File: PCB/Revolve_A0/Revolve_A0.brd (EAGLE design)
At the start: 100 x 100 mm, 409 parts, among them IC1 TMC2100-LA, IC12 TMC2100-LA, IC15 TMC2100-LA, IC2 TMC2100-LA, IC24 TMC2100-LA, IC29 LAN8710A, IC30 MTFC2GMDEA, IC31 CY7C65632, IC5 TMC2100-LA, IC6 74AHC1G126DCK, IC7 74AHC1G126DCK, Q1 AON6758, Q2 AON6758, Q3 AON6758, Q8 AON6758, U1 OSD3358-512M-BSM, U10 TPD4S012_DRY_6, U11 PCA9685PW, U19 CD4050BD, X1 22-05-7038-03, X10 22-05-7038-03, X11 22-05-7038-03, X12 22-05-7048-04, X13 22-05-7038-03, X14 22-05-7048-04, X15 22-05-7048-04, X16 22-05-7048-04, X17 22-05-7048-04, X18 22-05-7048-04, X19 22-05-7038-03, X2 MSTBA4, X20 MSTBA4, X21 MSTBA2, X22 22-05-7038-03, X24 HDMI, X25 22-05-7048-04, X26 MSTBA2, X29 22-05-7038-03, X3 MSTBA2, X4 22-05-7028-02, X5 22-05-7028-02, X6 22-05-7028-02, X7 22-05-7038-03, X8 22-05-7038-03, X9 22-05-7028-02, Y1 24MHz, Y3 25 MHz, Y4 12 MHz

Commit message: Working on the LAN layout
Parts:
- removed C106, C17, C19, C20, C22, C24, C27, C29, C31, C34, C43, C71: 0.1uF, rcl:C0402
- removed C116, C117, C118, C119, C120, C121, C122, C123, C124, C125, C126, C127, C128, C129, C130, C131: 47pF, rcl:C0402
- removed C139, C144, C145, C18, C21, C25, C36, C52, C62, C75, C76, C77, C78, C79, C81: 4.7uF, rcl:C0402
- removed C50: 10nF, rcl:C0402
- removed C90: 10uF, rcl:C0805
- removed C96: 100uF, Panasonic-EEEFK_EEEFP:RHS1V10MCN1GS
- removed IC1, IC12, IC15, IC2, IC24, IC5: TMC2100-LA, we-chip:QFN36-PAD
- removed IC31: CY7C65632, Revolve:QFN28
- removed R147: 0, DNI, rcl:R0402
- removed R148: 0, rcl:R0402
- removed R151: 10K, rcl:R0402
- removed R153: 22R, rcl:R0402
- removed R54, R86: 4.7K, rcl:R0402
- removed R91: 33, rcl:R0402
- removed U11: PCA9685PW, custom:SOP65P640X110-28N
- added C13: 0.1uF, rcl:C0402
- added C5: 18pF, rcl:C0402
- added H1, H2, H3, H4: MOUNT-HOLE3.2, holes:3,2
- added J1: (no value), OSD3358-SM-RED Platform:CTI-JTAG
- added Q9: MMBT2907, OSD3358-SM-RED Platform:SOT23-BEC
- added R143, R144: 4.7K, rcl:R0402
- added R26: 1M, rcl:R0402
- added SV3: (no value), con-lstb:MA04-2
- added SV4: (no value), con-lstb:MA03-1
- added SV5: (no value), con-lstb:MA04-1
- added U$13, U$14, U$15, U$16: TRINAMIC_TMC2130_QFN36, TMC2130-Eval_v13:TRINAMIC_QFN36
- added U2: TUSB2046BIRHBT, Texas Instruments_By_element14_Batch_1:QFN50P500X500X100-33N
- added U3, U4: TPD2E001DRSR, Texas Instruments_By_element14_Batch_1:SON95P315X315X80-7N
- added U5: SN74HC245DW, Texas Instruments_By_element14_Batch_1:SOIC127P1030X265-20N
- added U7: TLVH431, OSD3358-SM-RED Platform:SOT23-3
- added Y5: ABS07-32.768KHZ-T, OSD3358-SM-RED Platform:CRYSTAL_3.2X1.5
- C1: value 22nF -> 0.1uF
- C12, C138, C140, C141, C142: value 4.7uF -> 0.1uF
- C143: value 4.7uF -> 10uF
- C48, C80: value 10uF -> 22uF
- C6: value 0.1uF -> 18pF
- EEPROM_WP, PMIC_NRESET, SYS_5V, SYS_RTC_1V8, SYS_VDD1_3V3, SYS_VDD2_3V3, SYS_VDD3_3V3, VDDS_DDR, VDDS_PLL, VDD_CODE, VDD_MPU: value TPPAD1-13 -> TPB1,27; device testpad:P1-13 -> testpad:B1,27
- R1: value 0.1R -> 1.5K; device rcl:R0805 -> rcl:R0402
- R12: value 44.3K,1% -> 100K,1%
- R152: value 10K -> 10K,1%
- R2: value 0.1R -> 0,DNI; device rcl:R0805 -> rcl:R0402
- R22: value 10K,1% -> 13.3K,1%
- R24: value 4.7K -> 0R,DNI
- R41: value 10K -> 10K, 1%; device rcl:R0402 -> OSD3358-SM-RED Platform:R0402
- R49: value 10K -> 40.2K, 1%; device rcl:R0402 -> OSD3358-SM-RED Platform:R0402
- R53: value 2.2R -> 499; device rcl:R0402 -> OSD3358-SM-RED Platform:R0402
- R87: value 650R, 1% -> 4.7K
- SV2: device con-lstb:MA05-1 -> con-lstb:MA04-2
- U$9: value SN74AUC1G74DCTR -> TRINAMIC_TMC2130_QFN36; device Revolve:S-PDSO-G8 -> TMC2130-Eval_v13:TRINAMIC_QFN36
- Y1: value 24MHz -> 25MHz
- Y4: value 12 MHz -> 6 MHz
- moved PMIC_NRESET 474.8 mm to (44.7, 69.9), flipped to the bottom
- moved VDDS_PLL 452.8 mm to (38.5, 70.0), flipped to the bottom
- moved VDD_MPU 431.2 mm to (37.0, 70.0), flipped to the bottom
- moved VDD_CODE 397.7 mm to (38.8, 57.7), flipped to the bottom
- moved VDDS_DDR 376.0 mm to (37.3, 57.7), flipped to the bottom
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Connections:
- net N$1 renamed PMIC_PWR_EN
- net N$103 renamed PMIC_SCL
- net N$104 renamed PMIC_SDA
- net N$121 renamed PMIC_LDO_PGOOD
- net N$143 renamed PMIC_NWAKEUP
- net N$144 renamed PMIC_NINT
- net N$157 renamed TXP
- net N$158 renamed TXN
- net N$159 renamed RXP
- net N$160 renamed RXN
- net N$174 renamed EEPROM_WP
- net VBUS renamed USB_HOST_5V
- removed net 12MHZ: R91.1, U$7.27
- removed net D+: U$8.P$3, U10.1
- removed net D-: U$8.P$2, U10.2
- removed net ENABLE_A: IC24.22
- removed net ENABLE_E: IC12.22
- removed net ENABLE_H: IC15.22
- removed net ENABLE_X: IC1.22, U$2.22
- removed net ENABLE_Y: IC2.22
- removed net ENABLE_Z: IC5.22
- removed net END_STOP_X_1: U19.2
- removed net END_STOP_X_2: U19.10
- removed net END_STOP_Y_1: U19.4
- removed net END_STOP_Y_2: U19.12
- removed net END_STOP_Z_1: U19.6
- removed net END_STOP_Z_2: U19.15
- removed net FAULT_X0: U$2.20
- removed net FAULT_X1: U$2.21
- removed net I2C2_SCL: U11.26
- removed net I2C2_SDA: U11.27
- removed net ID: U$8.P$4, U10.3
- removed net IREF_A_RAW: R73.2, U11.8
- removed net IREF_E_RAW: R60.2, U11.21
- removed net IREF_H1: C81.1, R43.2, R73.1
- removed net IREF_H_RAW: R31.2, U11.22
- removed net IREF_X1: C145.1, R140.2, R141.1
- removed net IREF_X_RAW: R141.2, R41.2, U11.18
- removed net IREF_Y_RAW: R37.2, U11.19
- removed net IREF_Z_RAW: R58.2, U11.20
- removed net N$100: IC15.5
- removed net N$101: IC15.18
- removed net N$102: IC15.19
- removed net N$105: SYS_VDD1_3V3.TP, U1.F6, U1.F7, U1.G6, U1.G7
- removed net N$107: C70.1, IC15.26, R52.2
- removed net N$108: C71.1, IC1.26, R53.2
- removed net N$110: C72.1, IC2.26, R59.2
- removed net N$111: C74.1, IC12.26, R71.2
- removed net N$112: IC12.32, X17.1
- removed net N$119: IC15.32, X18.1
- removed net N$120: SYS_VDD3_3V3.TP, U1.F8, U1.G8, U1.H7, U1.H8, U1.J7, U1.J8, U1.K8, U1.L8
- removed net N$131: C52.1, IC24.23, R43.1
- removed net N$133: IC24.3
- removed net N$135: IC24.34, X25.2
- removed net N$136: C55.2, IC24.25, R72.1
- removed net N$138: IC24.4
- removed net N$139: IC24.5
- removed net N$140: IC24.18
- removed net N$141: IC24.19
- removed net N$142: SYS_RTC_1V8.TP, U1.K11, U1.L11
- removed net N$146: U1.F9, U1.G9, U1.H9, U1.J9, U1.K9, U1.L9
- removed net N$148: IC24.32, X25.1
- removed net N$165: U1.T7
- removed net N$166: C86.2, R126.1, U$2.25
- removed net N$175: R86.2
- removed net N$178: U1.T16
- removed net N$18: IC1.14, R1.2
- removed net N$185: C144.1, R140.1, U$2.23
- removed net N$186: U1.T12
- removed net N$187: C155.1, IC31.27, R147.1, R148.1
- removed net N$188: U1.R12
- removed net N$190: U1.T13
- removed net N$191: IC31.14, IC31.21, IC31.28, IC31.5, IC31.9
- removed net N$197: IC31.13, U$6.3
- removed net N$198: IC31.12, U$6.2
- removed net N$199: IC31.16, U$6.7
- removed net N$200: IC31.15, U$6.6
- removed net N$202: U$9.2, U$9.3
- removed net N$205: R91.2, U$9.5
- removed net N$210: SV2.5, U1.B12
- removed net N$213: C157.2, IC31.11, Y4.P$1
- removed net N$215: SV2.4, U1.A12
- removed net N$26: C25.1, IC5.23, R27.1
- removed net N$31: C21.2, IC1.25, R53.1
- removed net N$47: C33.2, IC2.25, R59.1
- removed net N$50: IC5.34, X16.2
- removed net N$51: C37.2, IC5.25, R70.1
- removed net N$53: IC2.5
- removed net N$54: IC5.4
- removed net N$55: IC5.5
- removed net N$56: IC2.18
- removed net N$57: IC5.18
- removed net N$58: IC5.19
- removed net N$60: C50.2, L1.P$2, U$10.2
- removed net N$65: IC2.19
- removed net N$73: C50.1, U$10.6
- removed net N$74: C62.1, IC12.23, R35.1
- removed net N$76: IC12.3
- removed net N$78: IC12.34, X17.2
- removed net N$79: C65.2, IC12.25, R71.1
- removed net N$81: IC12.4
- removed net N$82: IC12.5
- removed net N$83: IC12.18
- removed net N$84: IC12.19
- removed net N$89: C36.1, IC15.23, R50.1
- removed net N$91: IC15.3
- removed net N$94: IC15.34, X18.2
- removed net N$95: C68.2, IC15.25, R52.1
- removed net N$99: IC15.4
- removed net SPI0_CS0: U1.A14
- removed net SPI0_CS1: U1.C14
- removed net USB1_OCN: U1.R15
- removed net XDMA_EVENT_INTR0: U$9.1, U1.A4
- removed net X_CFG1: IC1.4
- removed net X_CFG2: IC1.3
- new net 5VIN_Y: C72.1, R59.2, U$13.26
- new net 5VOUT_A: C55.2, R72.1, R73.2, U$16.25
- new net 5VOUT_E: C65.2, R35.2, R71.1, U$14.25
- new net 5VOUT_H: C68.2, R31.2, R52.1, U$15.25
- new net 5VOUT_X: C86.2, R126.1, R140.2, U$2.25
- new net 5VOUT_Y: C33.2, R37.2, R59.1, U$13.25
- new net 5VOUT_Z: C37.2, R27.2, R70.1, U$9.25
- new net CLKOUT1_25MHZ: R2.1, U1.A4
- new net CLKOUT2_48MHZ: U1.B4, U2.27
- new net ECAP1: SV5.3, U1.B12
- new net ECAP2: SV5.2, U1.A12
- new net EHRPWM1A: U1.P12, U5.6
- new net EHRPWM1B: U1.T13, U5.7
- new net EHRPWM2A: U1.T4, U5.8
- new net EHRPWM2B: U1.P5, U5.9
- new net EMU0: J1.13, U1.E2
- new net EMU1: J1.14, U1.E3
- new net ENABLE_B: SV2.4
- new net ENABLE_C: SV3.3
- new net END_STOP_X1: U1.N14, U19.2
- new net END_STOP_X2: U1.R12, U19.10
- new net END_STOP_Y1: U1.T16, U19.4
- new net END_STOP_Y2: U1.P3, U19.12
- new net END_STOP_Z1: U1.T6, U19.6
- new net END_STOP_Z2: U1.P7, U19.15
- new net FAULT_A: R44.1, U$16.20, U$16.21
- new net FAULT_B: SV2.2
- new net FAULT_C: SV3.1
- new net GPIO0_18: U1.J15
- new net GPIO0_26: U1.R5
- new net I2C1_SCL: U1.B11
- new net I2C1_SDA: U1.A11
- new net N$1: R41.1, R49.2, U7.1
- new net N$25: R152.1, U1.M16
- new net QUAD_ENCODER_A: U1.R13
- new net QUAD_ENCODER_B: U1.P13
- new net SPI0_CSA: U$16.2, U1.J14
- new net SPI0_CSE: U$14.2, U1.T12
- new net SPI0_CSH: U$15.2, U1.R7
- new net SPI0_CSY: U$13.2, U1.C14
- new net SPI0_CSZ: U$9.2, U1.T7
- new net SPI1_CS0: SV3.4, U1.B10
- new net SPI1_CS1: SV2.3, U1.A10
- new net SPI1_MISO: SV2.6, SV3.6, U1.C12
- new net SPI1_MOSI: SV2.8, SV3.8, U1.C13
- new net SPI1_SCLK: SV2.1, SV3.2, U1.C5
- new net SW: C2.1, L1.P$2, U$10.2
- new net SYS_RTC_1V8: Q9.C, R49.1, SYS_RTC_1V8.TP, U1.K11, U1.L11, U7.3
- new net SYS_VDD1_3V3: C13.1, C140.1, C141.1, C142.1, C143.1, C150.1, C155.1, IC29.12, IC30.C6, IC30.E6, IC30.F5, IC30.J10, IC30.K9, IC30.M4, IC30.N4, IC30.P3, IC30.P5, L2.1, R1.2, R127.2, R128.2, R129.2, R130.2, R131.2, R132.2, R133.2, R134.2, R135.2, R136.2, R137.2, R24.1, R85.1, R88.2, SYS_VDD1_3V3.TP, U1.F6, U1.F7, U1.G6, U1.G7, U2.25, U2.26, U2.3
- new net SYS_VDD3_3V3: Q9.E, R41.2, R53.2, SYS_VDD3_3V3.TP, U1.F8, U1.F9, U1.G8, U1.G9, U1.H7, U1.H8, U1.H9, U1.J7, U1.J8, U1.J9, U1.K8, U1.K9, U1.L8, U1.L9
- new net TCK: J1.11, U1.D1
- new net TDI: J1.3, U1.C1
- new net TDO: J1.7, U1.C2
- new net TIMER4: U1.M1, U5.2
- new net TIMER5: U1.N3, U5.3
- new net TIMER6: U1.N2, U5.4
- new net TIMER7: U1.N1, U5.5
- new net TK_A: U1.D7
- new net TK_E: U1.C7
- new net TK_H: U1.C8
- new net TK_HBP: U1.C9
- new net TMS: J1.1, U1.D2
- new net TRSRTN: J1.2
- new net TRSTN: U1.D3
- new net UART4_RXD: SV4.1, U1.P15
- new net UART4_TXD: SV4.2, U1.R16
- new net USB1_DM3: U$6.2, U2.19, U4.3
- new net USB1_DM4: U$6.6, U2.23, U3.3
- new net USB1_DP3: U$6.3, U2.20, U4.6
- new net USB1_DP4: U$6.7, U2.24, U3.6
- new net USB_XTAL1: C157.2, U2.30, Y4.P$1
- new net VCC: U3.1, U4.1
- new net VCC_E: C74.1, R71.2, U$14.26
- new net VCC_H: C70.1, R52.2, U$15.26
- net +24V: now also C1.2, U$13.16, U$13.30, U$13.31, U$14.16, U$14.30, U$14.31, U$15.16, U$15.30, U$15.31, U$16.16, U$16.30, U$16.31, U$9.16, U$9.30, U$9.31; no longer C19.1, C20.2, C22.2, C24.1, C27.1, C29.1, C31.1, C34.1, C43.1, C6.1, C90.1, C96.+, IC1.16, IC1.30, IC1.31, IC12.16, IC12.30, IC12.31, IC15.16, IC15.30, IC15.31, IC2.16, IC2.30, IC2.31, IC24.16, IC24.30, IC24.31, IC5.16, IC5.30, IC5.31
- net +3V3: now also R143.1, R144.1, U$13.8, U$14.8, U$15.8, U$16.8; no longer C106.1, C2.1, IC1.8, IC12.8, IC15.8, IC2.8, IC24.8, IC5.8, R24.2, R54.2, U$9.6, U$9.7
- net +5V: no longer R147.2
- net CGND: now also U$3.SHD1, U$3.SHD2, U$5.A10, U$5.A11, U$5.A12, U$5.A9, U$6.A10, U$6.A11, U$6.A12, U$6.A9, U$8.P$10, U$8.P$11, U$8.P$6, U$8.P$7, U$8.P$8, U$8.P$9, X24.PAD1, X24.PAD2, X24.PAD3, X24.PAD4
- net DIR_A: now also U$16.7; no longer IC24.7
- net DIR_B: now also SV2.5
- net DIR_C: now also SV3.5
- net DIR_E: now also U$14.7; no longer IC12.7
- net DIR_H: now also U$15.7; no longer IC15.7
- net DIR_X: no longer IC1.7
- net DIR_Y: now also U$13.7; no longer IC2.7
- net DIR_Z: now also U$9.7; no longer IC5.7
- net EMMC_RST: no longer U1.R13
- net ENABLE: now also U5.19; no longer U11.23
- net FAN0: now also U5.14; no longer U11.13
- net FAN1: now also U5.13; no longer U11.15
- net FAN2: now also U5.12; no longer U11.16
- net FAN3: now also U5.11; no longer U11.17
- net FAULT_E: now also U$14.20, U$14.21; no longer IC12.20
- net FAULT_H: now also U$15.20, U$15.21; no longer IC15.20, IC24.20, R44.1
- net FAULT_X: now also R143.2, U$2.20, U$2.21, U1.T5; no longer IC1.20, R54.1
- net FAULT_Y: now also R144.2, U$13.20, U$13.21; no longer IC2.20, R24.1
- net FAULT_Z: now also U$9.20, U$9.21; no longer IC5.20
- net GND: now also C1.1, C13.2, J1.10, J1.12, J1.16, J1.20, J1.8, R141.1, R152.2, R43.1, R50.1, R58.1, R6.1, R60.1, SV4.3, SV5.1, U$13.1, U$13.11, U$13.12, U$13.17, U$13.22, U$13.24, U$13.35, U$13.36, U$13.9, U$13.GND_PAD, U$14.1, U$14.11, U$14.12, U$14.17, U$14.22, U$14.24, U$14.35, U$14.36, U$14.9, U$14.GND_PAD, U$15.1, U$15.11, U$15.12, U$15.17, U$15.22, U$15.24, U$15.35, U$15.36, U$15.9, U$15.GND_PAD, U$16.1, U$16.11, U$16.12, U$16.17, U$16.22, U$16.24, U$16.35, U$16.36, U$16.9, U$16.GND_PAD, U$2.22, U$2.9, U$9.1, U$9.11, U$9.12, U$9.17, U$9.22, U$9.24, U$9.35, U$9.36, U$9.9, U$9.GND_PAD, U2.28, U2.7, U2.8, U5.10; no longer C106.2, C116.2, C117.2, C118.2, C119.2, C120.2, C121.2, C122.2, C123.2, C124.2, C125.2, C126.2, C127.2, C128.2, C129.2, C130.2, C131.2, C139.2, C144.2, C145.2, C17.2, C18.2, C19.2, C2.2, C20.1, C21.1, C24.2, C25.2, C27.2, C29.2, C31.2, C34.2, C36.2, C43.2, C52.2, C6.2, C62.2, C71.2, C75.2, C76.2, C77.2, C78.2, C79.2, C81.2, C90.2, C96.-, IC1.1, IC1.10, IC1.11, IC1.12, IC1.24, IC1.35, IC1.36, IC1.TP, IC12.1, IC12.10, IC12.11, IC12.12, IC12.24, IC12.35, IC12.36, IC12.TP, IC15.1, IC15.10, IC15.11, IC15.12, IC15.24, IC15.35, IC15.36, IC15.TP, IC2.1, IC2.10, IC2.11, IC2.12, IC2.24, IC2.35, IC2.36, IC2.TP, IC24.1, IC24.10, IC24.11, IC24.12, IC24.24, IC24.35, IC24.36, IC24.TP, IC31.29, IC5.1, IC5.10, IC5.11, IC5.12, IC5.24, IC5.35, IC5.36, IC5.TP, R1.1, R151.1, R2.1, R86.1, SV2.1, U$5.A10, U$5.A11, U$5.A12, U$5.A9, U$6.A10, U$6.A11, U$6.A12, U$6.A9, U$8.P$10, U$8.P$11, U$8.P$6, U$8.P$7, U$8.P$8, U$8.P$9, U$9.4, U11.14
- net HDMI_1V8: now also C12.1
- net HDMI_INT: now also U1.R15; no longer U1.T15
- net HEATER_A: now also U5.15; no longer U11.12
- net HEATER_E: now also U5.18; no longer U1.P12
- net HEATER_H: now also U5.17; no longer U11.9
- net HEATER_HBP: now also U5.16; no longer U11.10
- net IREF_E: now also R35.1, R60.2, U$14.23; no longer C79.1, R35.2, R60.1
- net IREF_H: now also U$15.23; no longer C75.1
- net IREF_X: now also R140.1, R141.2, U$2.23; no longer C77.1, R41.1, R49.2
- net IREF_Y: now also U$13.23; no longer C76.1
- net IREF_Z: now also R27.1, R58.2, U$9.23; no longer C78.1, R27.2, R58.1
- net LCD_D0: no longer C116.1
- net LCD_D1: no longer C117.1
- net LCD_D10: no longer C126.1
- net LCD_D11: no longer C127.1
- net LCD_D12: no longer C128.1
- net LCD_D13: no longer C129.1
- net LCD_D14: no longer C130.1
- net LCD_D15: no longer C131.1
- net LCD_D2: no longer C118.1
- net LCD_D3: no longer C119.1
- net LCD_D4: no longer C120.1
- net LCD_D5: no longer C121.1
- net LCD_D6: no longer C122.1
- net LCD_D7: no longer C123.1
- net LCD_D8: no longer C124.1
- net LCD_D9: no longer C125.1
- net LCD_DE: no longer R153.2
- net LCD_PCLK: no longer R153.1
- net N$109: now also U$9.26; no longer IC5.26
- net N$113: now also U$15.13; no longer IC15.13
- net N$12: now also U$15.27; no longer IC15.27
- net N$126: now also U$16.14; no longer IC24.14
- net N$128: now also U$16.33; no longer IC24.33
- net N$13: now also U$15.14; no longer IC15.14
- net N$132: now also U$16.28; no longer IC24.28
- net N$134: now also U$16.15; no longer IC24.15
- net N$137: now also U$16.29; no longer IC24.29
- net N$14: now also U$9.27; no longer IC5.27
- net N$145: now also U$16.26; no longer IC24.26
- net N$147: now also U$16.13; no longer IC24.13
- net N$15: now also U$9.14; no longer IC5.14
- net N$16: now also U$9.32, X16.2; no longer C1.1, IC1.28
- net N$17: now also U2.10, U2.14, U2.18, U2.22; no longer C1.2, IC1.27
- net N$180: now also R2.2
- net N$19: now also U$13.32, X15.2; no longer IC1.33, R2.2
- net N$192: now also R24.2, U2.31; no longer IC31.8
- net N$193: now also U2.12; no longer IC31.4
- net N$194: now also U2.11; no longer IC31.3
- net N$195: now also U2.16; no longer IC31.7
- net N$196: now also U2.15; no longer IC31.6
- net N$2: now also U$13.13; no longer IC2.13
- net N$20: now also U$13.34, X15.1; no longer C12.1, IC1.23, R49.1
- net N$214: now also U2.29; no longer IC31.10
- net N$22: now also U$14.34, X17.1; no longer IC2.32, X15.1
- net N$24: now also U$9.33; no longer IC5.33
- net N$27: now also U$9.28; no longer IC5.28
- net N$28: now also U$14.32, X17.2; no longer IC5.3
- net N$29: now also U$9.15; no longer IC5.15
- net N$3: now also U$13.27; no longer IC2.27
- net N$30: now also U$15.33; no longer IC15.33
- net N$32: now also U$15.34, X18.1; no longer IC5.32, X16.1
- net N$33: now also C5.1, C6.1, U1.B5; no longer C22.1, IC1.29
- net N$35: now also U$13.14; no longer IC2.14
- net N$36: now also U$13.33; no longer IC2.33
- net N$37: now also U$9.13; no longer IC5.13
- net N$38: now also U$15.32, X18.2; no longer C18.1, IC2.23, R6.1
- net N$39: now also U$14.13; no longer IC12.13
- net N$4: now also Q9.B, R53.1, U7.2; no longer SV2.3, U1.C12
- net N$41: now also U$13.28; no longer IC2.28
- net N$42: now also C6.2, R26.2, U1.A5, Y5.P$2; no longer IC2.3
- net N$43: now also C5.2, R26.1, U1.A6, Y5.P$1; no longer IC1.19
- net N$44: now also U$16.34, X25.1; no longer IC1.5
- net N$45: now also U$13.15; no longer IC2.15
- net N$46: now also U$16.32, X25.2; no longer IC2.34, X15.2
- net N$48: now also U$13.29; no longer IC2.29
- net N$49: now also R43.2, R73.1, U$16.23; no longer IC2.4
- net N$5: now also C2.2, U$10.6; no longer SV2.2, U1.C13
- net N$52: now also U$9.29; no longer IC5.29
- net N$6: now also U$9.34, X16.1; no longer IC1.18
- net N$70: now also U$14.27; no longer IC12.27
- net N$71: now also U$14.14; no longer IC12.14
- net N$72: now also U$14.33; no longer IC12.33
- net N$75: now also U$14.28; no longer IC12.28
- net N$77: now also U$14.15; no longer IC12.15
- net N$80: now also U$14.29; no longer IC12.29
- net N$90: now also U$15.28; no longer IC15.28
- net N$92: now also U$15.15; no longer IC15.15
- net N$96: now also U$16.27; no longer IC24.27
- net N$98: now also U$15.29; no longer IC15.29
- net SPI0_CSX: now also U1.A14
- net SPI0_MISO: now also U$13.5, U$14.5, U$15.5, U$16.5, U$9.5
- net SPI0_MOSI: now also U$13.4, U$14.4, U$15.4, U$16.4, U$9.4
- net SPI0_SCLK: now also U$13.3, U$14.3, U$15.3, U$16.3, U$9.3
- net STEP_A: now also U$16.6; no longer IC24.6
- net STEP_B: now also SV2.7
- net STEP_C: now also SV3.7
- net STEP_E: now also U$14.6; no longer IC12.6
- net STEP_H: now also U$15.6; no longer IC15.6
- net STEP_X: no longer IC1.6
- net STEP_Y: now also U$13.6; no longer IC2.6
- net STEP_Z: now also U$9.6; no longer IC5.6
- net SYS_5V: now also U5.1, U5.20; no longer C17.1, R148.2, R88.2, U11.1, U11.2, U11.24, U11.28, U11.3, U11.4, U11.5
- net SYS_RESETN: now also U1.N12, U1.P11, U1.R11
- net SYS_VDD2_3V3: now also SV5.4
- net USB0_DM: now also U$8.P$2, U10.2
- net USB0_DP: now also U$8.P$3, U10.1
- net USB0_ID: now also U$8.P$4, U10.3
- net USB1_DM: now also U2.2; no longer IC31.1
- net USB1_DP: now also R1.1, U2.1; no longer IC31.2
- net USB_DC: no longer IC31.22, R151.2
- net USB_RESET: now also U2.4; no longer IC31.17
- net USR0: now also U1.T15; no longer U1.P13
- net VDD_3V3B: no longer C139.1, C140.1, C141.1, C142.1, C143.1, C150.1, IC29.12, IC30.C6, IC30.E6, IC30.F5, IC30.J10, IC30.K9, IC30.M4, IC30.N4, IC30.P3, IC30.P5, L2.1, R127.2, R128.2, R129.2, R130.2, R131.2, R132.2, R133.2, R134.2, R135.2, R136.2, R137.2, R85.1
- net X_A1: now also X14.1; no longer X14.2
- net X_A2: now also X14.2; no longer X14.1
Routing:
- net SPI0_MISO: track 0.00 -> 164.0 mm, vias 0 -> 7
- net FAN3: track 148.3 -> 0.00 mm, vias 2 -> 0
- net FAN2: track 141.6 -> 0.00 mm, vias 2 -> 0
- net FAN1: track 136.2 -> 0.00 mm, vias 2 -> 0
- net FAN0: track 135.4 -> 0.00 mm, vias 4 -> 0
- net SYS_RESETN: track 12.6 -> 141.1 mm, vias 0 -> 5
- net SPI0_MOSI: track 0.00 -> 125.8 mm, vias 0 -> 6
- net SPI0_SCLK: track 0.00 -> 121.9 mm, vias 0 -> 6
- net IREF_A_RAW: track 113.0 -> 0.00 mm, vias 4 -> 0
- net SYS_5V: track 94.9 -> 0.64 mm, vias 4 -> 1
- net IREF_H_RAW: track 82.0 -> 0.00 mm, vias 2 -> 0
- net N$125: track 1.12 -> 76.7 mm, vias 0 -> 2
- net N$124: track 1.18 -> 75.7 mm, vias 0 -> 2
- net N$123: track 1.18 -> 74.7 mm, vias 0 -> 2
- net N$201: track 0.00 -> 73.0 mm, vias 0 -> 2
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- added copper zone on layer 1, net +5V
- added copper zone on layer 3, net N$18
- added copper zone on layer 1, net SW
- added copper zone on layer 3, net SW
- added copper zone on layer 1, net SYS_5V
- added copper zone on layer 1, net SYS_RTC_1V8
- added copper zone on layer 1, net SYS_VDD1_3V3
- added copper zone on layer 3, net SYS_VDD1_3V3
- added copper zone on layer 1, net SYS_VDD2_3V3
- added copper zone on layer 1, net SYS_VDD3_3V3
- added copper zone on layer 1, net SYS_VDD_1V8
- added copper zone on layer 1, net USB_DC
- added copper zone on layer 1, net VIN_BAT
- removed copper zone on layer 3, net VDD_3V3B
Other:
- outline, holes or cut-outs redrawn

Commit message: Working on layout
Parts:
- removed C5, C6: 18pF, rcl:C0402
- removed R26, R84: 1M, rcl:R0402
- removed U5: SN74HC245DW, Texas Instruments_By_element14_Batch_1:SOIC127P1030X265-20N
- removed Y3: 25 MHz, Revolve:ECS-250-20-5PVX
- removed Y5: ABS07-32.768KHZ-T, OSD3358-SM-RED Platform:CRYSTAL_3.2X1.5
- added Y2: 25MHz, Revolve:445C33D24M00000
- moved C61 41.5 mm to (64.7, 90.0), turned to 270 degrees
- moved U19 36.5 mm to (59.0, 88.2), turned to 270 degrees
- moved C151 30.0 mm to (28.9, 66.0)
- moved C152 29.6 mm to (28.9, 64.9)
- moved C107 29.2 mm to (28.9, 63.8)
- moved C148 6.83 mm to (30.8, 82.2), turned to 270 degrees
- moved C149 5.30 mm to (30.8, 86.8), turned to 90 degrees
- moved R95 1.81 mm to (32.5, 77.1)
- moved R96 1.81 mm to (33.6, 77.1)
- moved R100 1.81 mm to (31.5, 77.1)
- moved R101 1.81 mm to (36.8, 77.1)
- moved R103 1.81 mm to (38.8, 77.1)
- moved R104 1.81 mm to (37.8, 77.1)
- moved R85 1.81 mm to (39.8, 77.1)
- moved R97 1.81 mm to (34.7, 77.1)
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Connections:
- removed net +3V3: C23.1, C30.1, C44.1, C53.1, C61.1, C63.1, C84.1, R114.2, R117.2, R118.2, R119.2, R120.2, R143.1, R144.1, R28.2, R36.2, R44.2, R51.2, U$13.8, U$14.8, U$15.8, U$16.8, U$2.8, U$9.8, U19.1
- removed net ENABLE: U5.19
- removed net N$33: C5.1, C6.1, U1.B5
- removed net N$42: C6.2, R26.2, U1.A5, Y5.P$2
- removed net N$43: C5.2, R26.1, U1.A6, Y5.P$1
- net EHRPWM1A: no longer U5.6
- net EHRPWM1B: no longer U5.7
- net EHRPWM2A: no longer U5.8
- net EHRPWM2B: no longer U5.9
- net FAN0: no longer U5.14
- net FAN1: no longer U5.13
- net FAN2: no longer U5.12
- net FAN3: no longer U5.11
- net GND: now also X11.3, X7.3, X8.3; no longer U5.10
- net HEATER_A: no longer U5.15
- net HEATER_E: no longer U5.18
- net HEATER_H: no longer U5.17
- net HEATER_HBP: no longer U5.16
- net N$151: now also X11.2
- net N$180: now also Y2.P$2; no longer R84.2, Y3.P$2
- net N$181: now also Y2.P$1; no longer Y3.P$1
- net N$183: no longer R84.1
- net N$237: now also X8.2
- net N$241: now also X7.2
- net SYS_5V: no longer U5.1, U5.20
- net SYS_VDD1_3V3: now also C23.1, C30.1, C44.1, C53.1, C61.1, C63.1, C84.1, R114.2, R117.2, R118.2, R119.2, R120.2, R143.1, R144.1, R28.2, R36.2, R44.2, R51.2, U$13.8, U$14.8, U$15.8, U$16.8, U$2.8, U$9.8, U19.1
- net TIMER4: no longer U5.2
- net TIMER5: no longer U5.3
- net TIMER6: no longer U5.4
- net TIMER7: no longer U5.5
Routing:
- net SYS_VDD1_3V3: track 41.1 -> 160.0 mm, vias 19 -> 31
- net +3V3: track 118.3 -> 0.00 mm, vias 12 -> 0
- net TERM_A: track 0.00 -> 51.7 mm, vias 0 -> 2
- net SPI0_SCLK: track 121.9 -> 169.1 mm, vias 6 -> 7
- net SPI0_MOSI: track 125.8 -> 170.6 mm, vias 6 -> 8
- net SPI0_CSX: track 15.7 -> 58.2 mm, vias 0 -> 2
- net N$155: track 80.5 -> 40.9 mm
- net TERM_HBP: track 0.00 -> 33.1 mm, vias 0 -> 1
- net END_STOP_Z_2_IN: track 2.31 -> 30.1 mm, vias 0 -> 1
- net END_STOP_Y_2_IN: track 2.94 -> 26.9 mm, vias 0 -> 2
- net STEP_E: track 38.3 -> 61.8 mm, vias 0 -> 2
- net END_STOP_X_1_IN: track 3.59 -> 23.7 mm
- net MII1_TXD3: track 0.00 -> 17.6 mm, vias 0 -> 2
- net MII1_TXEN: track 0.00 -> 17.2 mm, vias 0 -> 2
- net END_STOP_X_2_IN: track 2.27 -> 19.4 mm, vias 0 -> 2
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- added copper zone on layer 3, net VDD_ADC
- removed copper zone on layer 3, net +3V3

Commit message: Almost done with schematic
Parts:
- removed C104, C105: 0.1uF, rcl:C0402
- removed F1: FUSE, fuse:3557
- removed FH1, FH2: FUSE-HOLDER, Replicape_Rev_B0:FUSE-HOLDER
- removed LED8: blue, led:CHIP-LED0603
- removed RT1: (no value), rcl:0204/5
- removed U$11, U$12: DF10G7M1N, Revolve:DF10G7M1N
- added C14, C17: 22uF, rcl:C1206
- added C18, C19, C5, C6: 0.1uF, rcl:C0402
- added Q10, Q11, Q13, Q14: DMC2038LVT, Manga_screen_rev_B:TSOT26
- added Q12: (no value), semicon-smd-ipc:SOT23
- added R142, R54, R91: 4.7K, rcl:R0402
- added R26: 0.001,1%, resistor:R2512
- added R84, R86: 100K,1%, rcl:R0402
- added U$17: SISS27DN, Revolve:POWERPAK-1212-8S
- added U$18: TPD12S016-RKT, Revolve:R-PDSO-G24
- added U11: SN74AHC595PW, Replicape_B3:SOP65P640X120-16N
- added U5: UA78L05ACD, Texas Instruments_By_element14_Batch_1:SOIC127P600X175-8N
- added U6, U8, U9: TPD4S012_DRY_6_P1_P, OSD3358-SM-RED Platform:DRY6
- C148, C149: value 30pF -> 18pF
- R1: value 1.5K -> 10K
- R105, R106, R107, R108, R109, R110, R111, R112, R113, R114, R115, R116, R117, R118, R119, R120: value 100K -> 100K,1%
- R2: value 0,DNI -> 0R,DNI
- R45: value 4.7K -> 100K,1%
- R55, R56, R57: value 4.7K -> 10K
- U3: value TPD2E001DRSR -> TPS2061D; device Texas Instruments_By_element14_Batch_1:SON95P315X315X80-7N -> Texas Instruments_By_element14_Batch_1:SOIC127P600X175-8N
- U4: value TPD2E001DRSR -> TPD4S012_DRY_6_P1_P; device Texas Instruments_By_element14_Batch_1:SON95P315X315X80-7N -> OSD3358-SM-RED Platform:DRY6
- X24: value HDMI -> HDMI4; device hdmi:HDMI-C -> hdmi:HDMI-A-TH
- moved R93 97.4 mm to (15.2, 88.8)
- moved R92 97.4 mm to (15.2, 89.8)
- moved R55 65.4 mm to (29.0, 93.8)
- moved R1 55.2 mm to (37.2, 94.0)
- moved R56 48.7 mm to (20.6, 94.0)
- moved L2 36.3 mm to (32.4, 89.0)
- moved R57 29.7 mm to (11.9, 94.0)
- moved R122 26.9 mm to (45.1, 90.5), turned to 90 degrees
- moved R125 26.3 mm to (46.8, 88.2)
- moved D5 26.0 mm to (19.1, 35.8)
- moved R80 23.9 mm to (95.6, 74.7), turned to 180 degrees
- moved R124 23.0 mm to (47.9, 87.3)
- moved R79 17.7 mm to (91.4, 92.8), turned to 180 degrees
- moved R76 17.2 mm to (25.3, 89.2), turned to 180 degrees
- moved R16 13.5 mm to (11.6, 58.7), turned to 90 degrees
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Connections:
- net N$152 renamed VDDCR
- net N$25 renamed RTC_KALDO_ENN
- net TK_HBP renamed I_MEASURE
- removed net DDC/CEC-GRND: X24.17
- removed net ECAP1: SV5.3, U1.B12
- removed net ECAP2: SV5.2, U1.A12
- removed net EHRPWM1A: U1.P12
- removed net EHRPWM1B: U1.T13
- removed net EHRPWM2A: U1.T4
- removed net EHRPWM2B: U1.P5
- removed net GPIO0_18: U1.J15
- removed net GPIO0_26: U1.R5
- removed net N$17: U2.10, U2.14, U2.18, U2.22
- removed net N$193: U$5.3, U2.12
- removed net N$194: U$5.2, U2.11
- removed net N$195: U$5.7, U2.16
- removed net N$196: U$5.6, U2.15
- removed net SPI0_CSE: U$14.2, U1.T12
- removed net SPI0_CSH: U$15.2, U1.R7
- removed net SPI0_CSX: U$2.2, U1.A14
- removed net SPI0_CSY: U$13.2, U1.C14
- removed net SPI0_CSZ: U$9.2, U1.T7
- removed net TIMER4: U1.M1
- removed net TIMER5: U1.N3
- removed net TIMER6: U1.N2
- removed net TIMER7: U1.N1
- removed net TK_A: U1.D7
- removed net USB_HOST_5V: U$5.1, U$5.5, U$6.1, U$6.5
- removed net VCC: U3.1, U4.1
- new net +12V: C5.2, U5.1, X12.4
- new net +24V_FOR_5V: C1.2, C47.1, D5.C, U$10.3
- new net ENABLE_STUFF: Q12.1, R91.1, U1.J15
- new net EN_TK_A: Q14.1, Q14.3, R142.2, U11.3, X11.1
- new net EN_TK_E: Q10.1, Q10.3, R76.2, U11.15, X29.1
- new net EN_TK_H: Q11.1, Q11.3, R92.2, U11.1, X7.1
- new net EN_TK_HBP: Q13.1, Q13.3, R93.2, U11.2, X8.1
- new net MGND: C102.2, C57.2, C58.2, C59.2, LED1.C, LED2.C, LED3.C, LED4.C, Q1.1, Q1.2, Q1.3, Q2.1, Q2.2, Q2.3, Q3.1, Q3.2, Q3.3, Q8.1, Q8.2, Q8.3, R26.2, R46.1, R47.1, R48.1, R75.1
- new net N$26: R84.2, R86.1, U$17.G
- new net N$31: U$18.P$10, X24.19
- new net N$33: Q10.6, R1.1
- new net N$47: Q10.4, R18.2
- new net N$50: Q13.6, R56.1
- new net N$53: Q14.6, R57.1
- new net N$55: U$18.P$9, X24.16
- new net N$56: U$18.P$8, X24.15
- new net N$57: U$18.P$7, X24.13
- new net N$58: Q11.4, R17.2
- new net N$59: Q13.4, R13.2
- new net N$60: Q14.4, R77.2
- new net N$65: Q11.6, R55.1
- new net SPI0_CS0: U$13.2, U$14.2, U$15.2, U$16.2, U$2.2, U$9.2, U1.A14
- new net SPI0_CS1: U1.C14, U11.12
- new net SPI0_MISO_E: U$14.5, U$15.4
- new net SPI0_MISO_H: U$15.5, U$16.4
- new net SPI0_MISO_X: U$13.4, U$2.5
- new net SPI0_MISO_Y: U$13.5, U$9.4
- new net SPI0_MISO_Z: U$14.4, U$9.5
- new net USB1_DM1: U$5.2, U2.11, U9.1
- new net USB1_DM2: U$5.6, U2.15, U6.1
- new net USB1_DP1: U$5.3, U2.12, U9.2
- new net USB1_DP2: U$5.7, U2.16, U6.2
- new net USB1_DRVVBUS: U1.M14
- new net USB_OC: U2.10, U2.14, U2.18, U2.22, U3.5
- new net USB_PWR: U2.9, U3.2, U3.3
- new net USB_VBUS: C14.1, C17.1, U$5.1, U$5.5, U$6.1, U$6.5, U3.6, U3.7, U3.8, U4.6, U6.6, U8.6, U9.6
- new net VIN_MEASURE: R45.2, R54.1, U1.D7
- net +24V: now also C6.2, U$17.S1, U$17.S2, U$17.S3, U5.8; no longer C1.2, C47.1, D5.C, F1.P$3, F1.P$4, R14.2, R15.2, R16.2, R45.1, R55.2, R56.2, R57.2, R74.2, R76.2, U$10.3, X12.4
- net +5V: now also C18.2, C19.1, U$18.P$11, U1.M15, U11.10, U11.16, U3.4
- net CGND: now also X24.P$1, X24.P$2, X24.P$3, X24.P$4; no longer X24.PAD1, X24.PAD2, X24.PAD3, X24.PAD4
- net DVI_+5V: now also U$18.P$13; no longer R92.2, R93.2, RT1.2
- net ENABLE_B: now also SV2.3, U1.T7; no longer SV2.4
- net ENABLE_C: now also U1.R7
- net FAN0: now also U1.P12
- net FAN1: now also U1.T13
- net FAN2: now also U1.T4
- net FAN3: now also U1.P5
- net FAULT_B: now also SV2.1, U1.T12; no longer SV2.2
- net FAULT_C: now also U1.R5
- net GND: now also C14.2, C17.2, C18.1, C19.2, C5.1, C6.1, Q10.5, Q11.5, Q12.2, Q13.5, Q14.5, R142.1, R26.1, R54.2, R76.1, R91.2, R92.1, R93.1, U$18.P$14, U$18.P$19, U$18.P$6, U1.L14, U11.13, U11.8, U3.1, U4.4, U5.2, U5.3, U5.6, U5.7, U6.4, U8.4, U9.4, X24.17; no longer C102.2, C104.2, C105.1, C57.2, C58.2, C59.2, D5.A, Q1.1, Q1.2, Q1.3, Q2.1, Q2.2, Q2.3, Q3.1, Q3.2, Q3.3, Q8.1, Q8.2, Q8.3, R46.1, R47.1, R48.1, R75.1, U$11.3, U$12.3
- net HDMI_HPD: now also U$18.P$4; no longer X24.19
- net HEATER_A: now also R74.2, U1.N1
- net HEATER_E: now also R15.2, U1.M1
- net HEATER_H: now also R14.2, U1.N3
- net HEATER_HBP: now also R16.2, U1.N2
- net N$150: no longer LED4.C, R76.1
- net N$169: now also U$18.P$1; no longer X24.13
- net N$207: now also U$18.P$2; no longer R92.1, X24.15
- net N$208: now also U$18.P$3; no longer R93.1, X24.16
- net N$234: no longer LED3.C, R55.1
- net N$242: no longer LED2.C, R56.1
- net N$64: no longer LED1.C, R57.1
- net N$8: now also Q12.3, R86.2; no longer LED8.C, R45.2
- net QUAD_ENCODER_A: now also SV5.3
- net QUAD_ENCODER_B: now also SV5.2
- net SERVO_0: now also U1.B12
- net SERVO_0_EN: now also U11.4
- net SERVO_1: now also U1.A12
- net SERVO_1_EN: now also U11.5
- net SPI0_CSA: no longer U$16.2
- net SPI0_MISO: no longer U$13.5, U$14.5, U$15.5, U$2.5, U$9.5
- net SPI0_MOSI: now also U11.14; no longer U$13.4, U$14.4, U$15.4, U$16.4, U$9.4
- net SPI0_SCLK: now also U11.11
- net SPI1_CS1: now also SV2.4; no longer SV2.3
- net SPI1_SCLK: now also SV2.2; no longer SV2.1
- net SYS_5V: no longer RT1.1, X11.1, X29.1, X7.1, X8.1
- net SYS_RESETN: no longer C105.2
- net SYS_VDD1_3V3: now also SV5.4, U$18.P$24; no longer R1.2
- net SYS_VDD2_3V3: no longer SV5.4
- net TERM_A: now also R57.2
- net TERM_E: now also R1.2
- net TERM_H: now also R56.2
- net TERM_HBP: now also R55.2
- net TX0+: now also U$18.P$18; no longer U$12.5, U$12.6
- net TX0-: now also U$18.P$17; no longer U$12.4, U$12.7
- net TX1+: now also U$18.P$21; no longer U$11.2, U$11.9
- net TX1-: now also U$18.P$20; no longer U$11.1, U$11.10
- net TX2+: now also U$18.P$23; no longer U$11.5, U$11.6
- net TX2-: now also U$18.P$22; no longer U$11.4, U$11.7
- net TXC+: now also U$18.P$16; no longer U$12.2, U$12.9
- net TXC-: now also U$18.P$15; no longer U$12.1, U$12.10
- net USB1_DM3: now also U4.1; no longer U4.3
- net USB1_DM4: now also U8.1; no longer U3.3
- net USB1_DP: no longer R1.1
- net USB1_DP3: now also U4.2; no longer U4.6
- net USB1_DP4: now also U8.2; no longer U3.6
- net USB_DC: no longer C104.1
- net VDD_ADC: now also Q10.2, Q11.2, Q13.2, Q14.2; no longer R13.2, R17.2, R18.2, R77.2
- net VIN: now also D5.A, R45.1, R84.1, U$17.D1, U$17.D2, U$17.D3, U$17.D4, U$17.D5; no longer F1.P$1, F1.P$2, LED8.A
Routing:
- net SPI0_CS0: track 0.00 -> 169.1 mm, vias 0 -> 8
- net SPI0_MISO: track 164.0 -> 36.8 mm, vias 7 -> 1
- net USB0_DP: track 0.00 -> 111.5 mm, vias 0 -> 2
- net SPI0_MOSI: track 170.6 -> 83.1 mm, vias 8 -> 3
- net STEP_H: track 13.3 -> 99.8 mm, vias 0 -> 2
- net N$179: track 3.72 -> 88.2 mm, vias 0 -> 2
- net USB0_DM: track 25.6 -> 109.1 mm, vias 1 -> 2
- net SERVO_1: track 0.00 -> 81.0 mm, vias 0 -> 2
- net FAN1: track 0.00 -> 79.5 mm, vias 0 -> 2
- net FAN3: track 0.00 -> 78.9 mm, vias 0 -> 4
- net SERVO_0: track 0.00 -> 76.4 mm, vias 0 -> 2
- net VIN_MEASURE: track 0.00 -> 75.5 mm, vias 0 -> 2
- net HEATER_A: track 16.7 -> 91.7 mm, vias 2 -> 4
- net N$156: track 0.00 -> 73.7 mm, vias 0 -> 2
- net SPI0_CSH: track 71.7 -> 0.00 mm, vias 2 -> 0
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- added copper zone on layer 3, net +12V
- added copper zone on layer 1, net +24V_FOR_5V
- added copper zone on layer 1, net CGND
- added copper zone on layer 1, net N$242
- added copper zone on layer 3, net N$42
- added copper zone on layer 3, net USB_DC
- removed copper zone on layer 3, net N$18

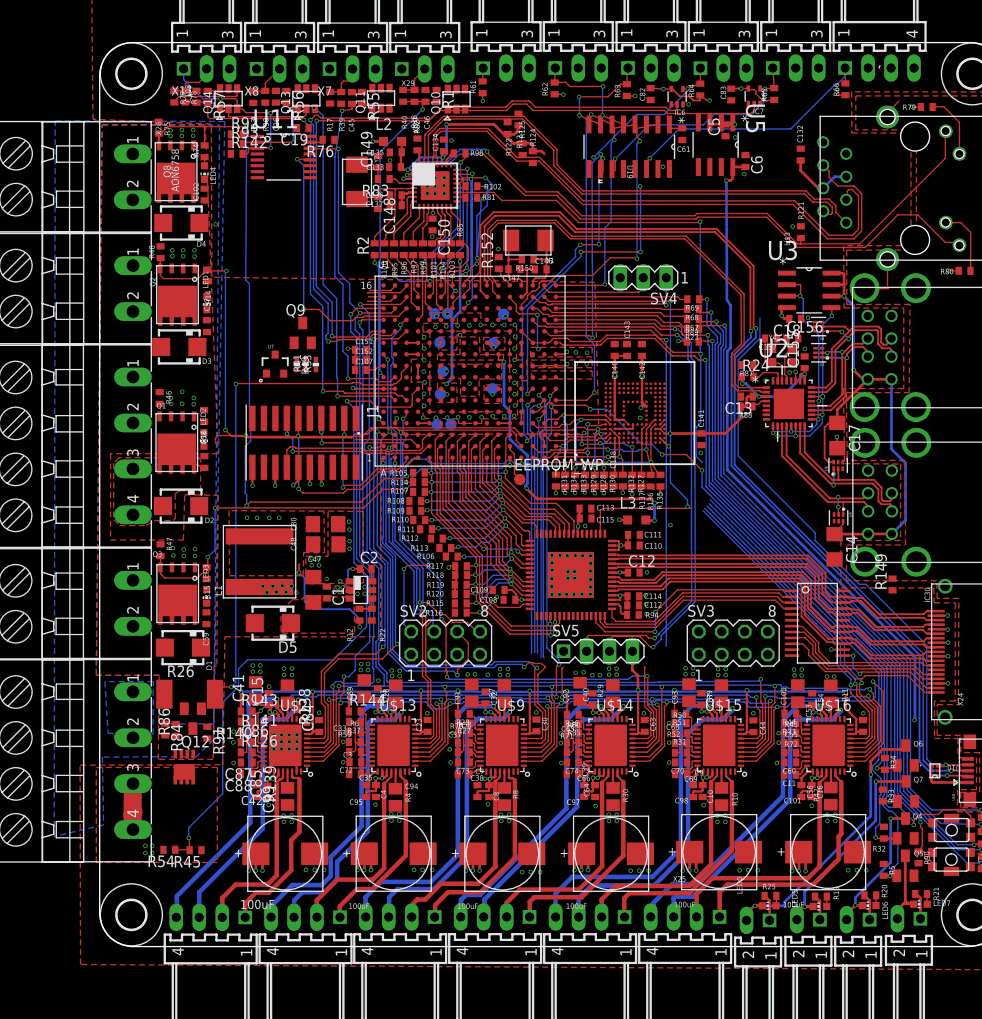
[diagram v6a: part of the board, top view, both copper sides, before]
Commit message: Almost done routing. Switched to high side measurement of current
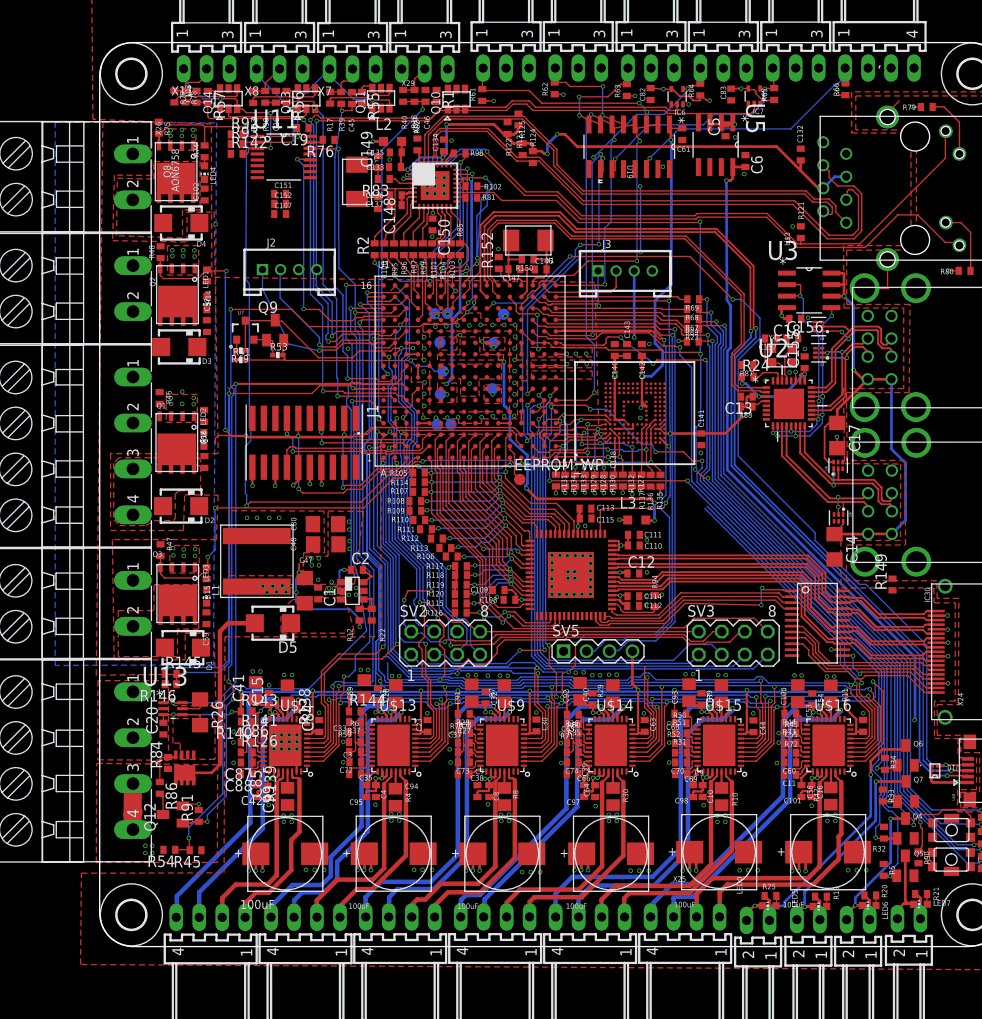
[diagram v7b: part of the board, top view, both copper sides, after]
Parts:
- removed SV4: (no value), con-lstb:MA03-1
- added C20: 0.1uF, rcl:C0402
- added J2, J3: 4P-2.0, Seeed-Connector:HW4-2.0
- added R145: 4.7K,1%, rcl:R0402
- added R146: 47k,NTC, rcl:R0402
- added U13: INA199A1DCKR, Texas Instruments_By_element14_Batch_1:SOT65P210X110-6N
- R26: device resistor:R2512 -> resistor:R1206
- moved C107 19.4 mm to (19.9, 81.0)
- moved C151 19.4 mm to (19.9, 83.2)
- moved C152 19.4 mm to (19.9, 82.1)
- moved Q12 10.8 mm to (8.10, 14.6), turned to 90 degrees
- moved R91 9.25 mm to (10.9, 14.4), turned to 90 degrees
- moved R41 7.16 mm to (15.6, 64.8), turned to 0 degrees
- moved R86 6.63 mm to (6.65, 17.6), turned to 270 degrees
- moved R49 6.39 mm to (15.6, 65.9), turned to 180 degrees
- moved U7 5.00 mm to (16.1, 68.1)
- moved R53 4.33 mm to (19.7, 65.4), turned to 0 degrees
- moved R84 3.71 mm to (7.55, 20.3), turned to 90 degrees
- moved Q9 3.06 mm to (19.4, 68.2)
- moved R94 2.86 mm to (61.4, 38.2), turned to 90 degrees
- moved R26 2.31 mm to (11.1, 25.9), turned to 270 degrees
- moved C1 0.96 mm to (24.1, 39.0)
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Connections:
- net SPI0_CSA renamed UNUSED_1
- removed net MGND: C102.2, C57.2, C58.2, C59.2, LED1.C, LED2.C, LED3.C, LED4.C, Q1.1, Q1.2, Q1.3, Q2.1, Q2.2, Q2.3, Q3.1, Q3.2, Q3.3, Q8.1, Q8.2, Q8.3, R26.2, R46.1, R47.1, R48.1, R75.1
- removed net TK_E: U1.C7
- new net P-SHUNT: R26.2, U$17.S1, U$17.S2, U$17.S3, U13.4
- new net THERM_BOARD: R145.2, R146.1, U1.C7
- net +24V: now also R26.1, U13.5; no longer U$17.S1, U$17.S2, U$17.S3
- net GND: now also C102.2, C20.1, C57.2, C58.2, C59.2, J2.4, J3.4, LED1.C, LED2.C, LED3.C, LED4.C, Q1.1, Q1.2, Q1.3, Q2.1, Q2.2, Q2.3, Q3.1, Q3.2, Q3.3, Q8.1, Q8.2, Q8.3, R114.2, R146.2, R46.1, R47.1, R48.1, R75.1, U13.1, U13.2; no longer R105.1, R26.1, SV4.3
- net I2C1_SCL: now also J2.1
- net I2C1_SDA: now also J2.2
- net I_MEASURE: now also U13.6
- net SYS_VDD1_3V3: now also C20.2, R105.1, U13.3; no longer R114.2
- net SYS_VDD2_3V3: now also J2.3, J3.3
- net UART4_RXD: now also J3.1; no longer SV4.1
- net UART4_TXD: now also J3.2; no longer SV4.2
- net VDD_ADC: now also R145.1
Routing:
- net ENABLE_STUFF: track 0.00 -> 91.4 mm, vias 0 -> 6
- net SPI1_CS0: track 0.00 -> 68.3 mm, vias 0 -> 2
- net DIR_A: track 34.7 -> 100.3 mm, vias 1 -> 2
- net THERM_BOARD: track 0.00 -> 58.1 mm, vias 0 -> 1
- net VDD_ADC: track 17.9 -> 66.5 mm, vias 2 -> 4
- net DIR_H: track 36.5 -> 82.1 mm, vias 2 -> 3
- net DIR_B: track 3.26 -> 48.1 mm
- net STEP_B: track 3.09 -> 47.0 mm
- net FAULT_B: track 46.5 -> 90.1 mm, vias 1 -> 3
- net SYS_VDD1_3V3: track 208.3 -> 250.8 mm, vias 36 -> 39
- net FAN0: track 40.4 -> 76.2 mm, vias 1 -> 2
- net USB0_ID: track 65.4 -> 100.8 mm, vias 1 -> 4
- net SYS_RTC_1V8: track 2.18 -> 35.6 mm, vias 1 -> 3
- net SPI1_SCLK: track 29.2 -> 62.2 mm, vias 3 -> 4
- net SPI1_MOSI: track 42.0 -> 74.8 mm
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- added copper zone on layer 1, net N$150
- added copper zone on layer 1, net N$234
- added copper zone on layer 1, net P-SHUNT
- removed copper zone on layer 16, net GND
- removed copper zone on layer 3, net SYS_5V
